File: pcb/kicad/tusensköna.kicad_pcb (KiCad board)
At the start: 2 copper layers, 93.2 x 50.5 mm, 36 parts, among them J1 AudioJack3, J2 AudioJack3, J3 Micro_SD_Card, SW1 SW_Push, SW2 SW_Push, U1 Electrosmith_Daisy_Seed_Rev4

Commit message: issues fixed
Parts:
- removed 3V3A1, 3V3D1, A0, A6, GND1, MI1, MO1, SCK1, SCL1, SDA1, SS1, VIN1: Conn_01x01, Connector_Wire:SolderWire-0.5sqmm_1x01_D0.9mm_OD2.1mm
- added J4: Conn_01x12_Pin, Connector_PinHeader_2.54mm:PinHeader_1x12_P2.54mm_Vertical, F.Cu at (156.0, 26.0)
- added JP1: Jumper_2_Bridged, Connector_PinHeader_2.54mm:PinHeader_1x02_P2.54mm_Vertical, F.Cu at (164.5, 28.6)
- added JP2: Jumper_2_Bridged, Connector_PinHeader_2.54mm:PinHeader_1x02_P2.54mm_Vertical, F.Cu at (160.7, 28.6)
- added R10: 4.7k, Resistor_SMD:R_0805_2012Metric, B.Cu at (143.3, 33.7)
- added R9: 4.7k, Resistor_SMD:R_0805_2012Metric, B.Cu at (145.9, 33.8)
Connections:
- U1 pad 12: /SDA -> Net-(JP1-A)
- U1 pad 13: /SCL -> Net-(JP2-A)
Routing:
- net Net-(JP1-A): track 0.00 -> 48.7 mm
- net Net-(JP2-A): track 0.00 -> 48.6 mm, vias 0 -> 1
- net /SDA: track 17.4 -> 37.4 mm
- net /SCL: track 17.8 -> 26.8 mm
- net /SPI_CS: track 15.8 -> 20.7 mm
- net /SPI_SCK: track 16.2 -> 20.4 mm
- net /SPI_POCI: track 16.6 -> 19.1 mm
- net /SPI_PICO: track 17.0 -> 19.4 mm
- net /VIN: track 60.5 -> 62.7 mm
- net /3V3D: track 107.5 -> 108.4 mm
- net /ADC6: track 44.1 -> 43.5 mm

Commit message: pullup
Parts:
- R10, R9: moved to F.Cu
- moved R9 18.6 mm to (164.5, 33.7), turned to -90 degrees
- moved R10 17.3 mm to (160.7, 33.7), turned to -90 degrees
- moved JP1 2.54 mm to (164.5, 26.0), turned to 0 degrees
- moved JP2 2.54 mm to (160.7, 26.0), turned to 0 degrees
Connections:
- JP1 pad 1: Net-(JP1-A) -> /3V3D
- JP1 pad 2: /SCL -> Net-(JP1-B)
- JP2 pad 1: Net-(JP2-A) -> /3V3D
- JP2 pad 2: /SDA -> Net-(JP2-B)
- R10 pad 1: Net-(JP2-A) -> Net-(JP2-B)
- R9 pad 1: Net-(JP1-A) -> Net-(JP1-B)
- U1 pad 12: Net-(JP1-A) -> /SCL
- U1 pad 13: Net-(JP2-A) -> /SDA
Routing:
- net Net-(JP1-A): track 48.7 -> 0.00 mm
- net Net-(JP2-A): track 48.6 -> 0.00 mm, vias 1 -> 0
- net /3V3D: track 108.4 -> 138.8 mm
- net /SDA: track 37.4 -> 26.5 mm
- net Net-(JP1-B): track 0.00 -> 4.17 mm
- net Net-(JP2-B): track 0.00 -> 4.16 mm

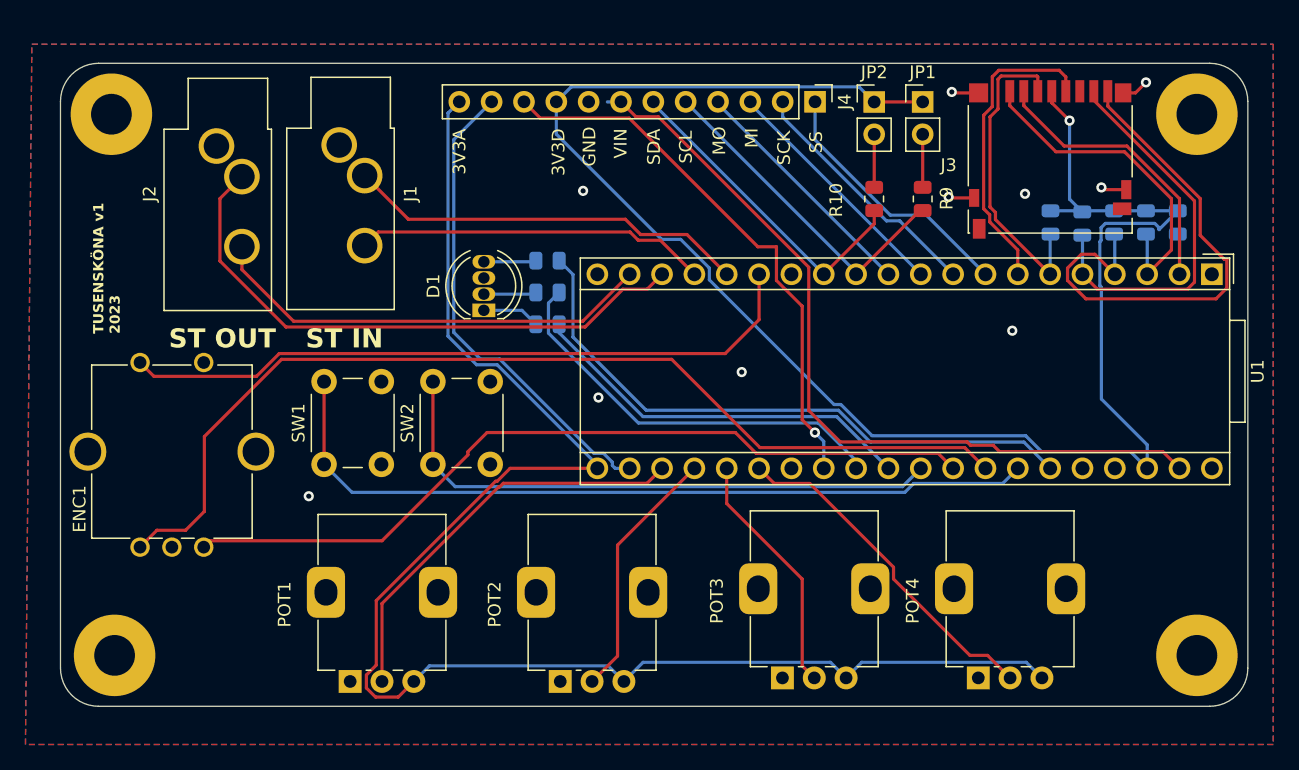
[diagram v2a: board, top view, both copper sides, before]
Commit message: fixed gnd planes and cleanup
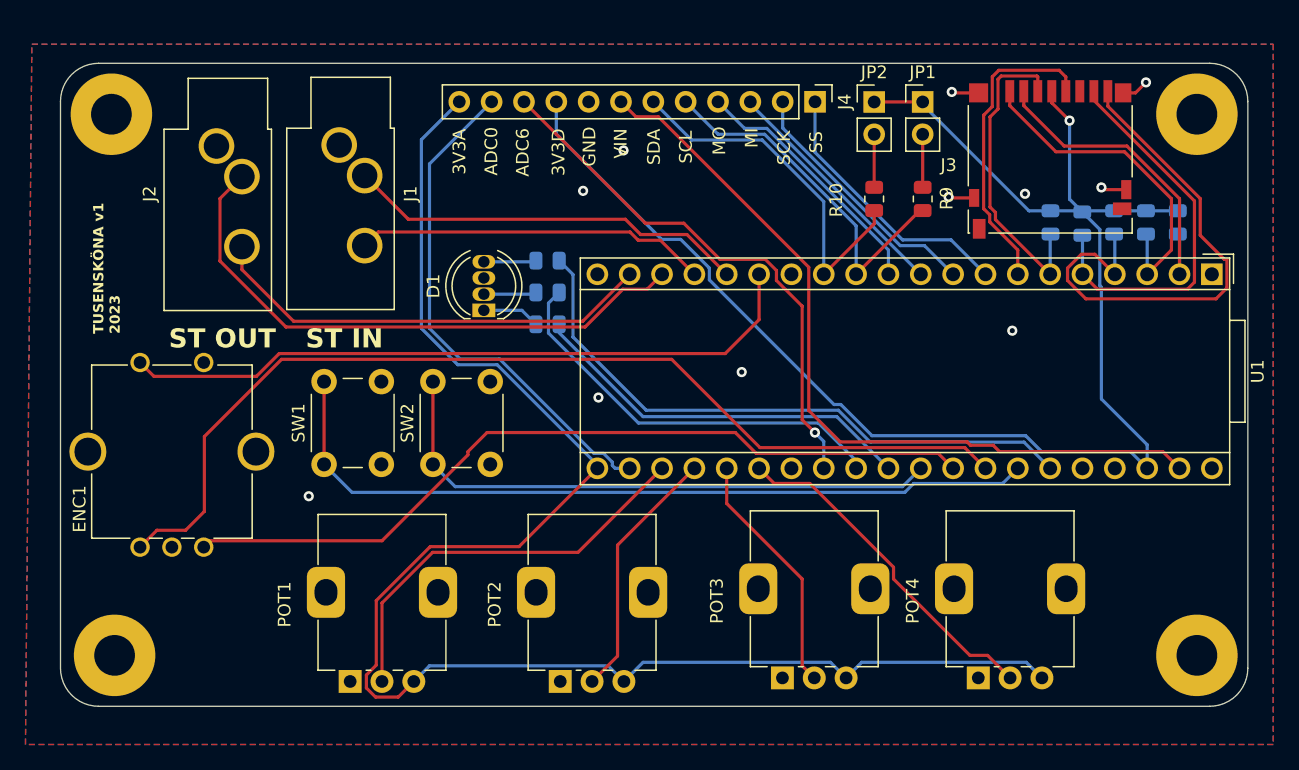
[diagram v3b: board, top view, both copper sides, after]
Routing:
- net /3V3D: track 138.8 -> 121.3 mm
- net /SDA: track 26.5 -> 29.1 mm
- net /3V3A: track 120.8 -> 123.4 mm
- net /ADC0: track 37.7 -> 40.2 mm
- net /SCL: track 26.7 -> 28.5 mm
- net /ADC6: track 43.5 -> 42.4 mm
- net /SPI_PICO: track 19.4 -> 20.3 mm
- net /SPI_CS: track 20.7 -> 21.3 mm
- net /SPI_SCK: track 20.4 -> 20.9 mm
- net /AGND: vias 10 -> 11
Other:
- board text added: "ADC0"
- board text added: "ADC6"

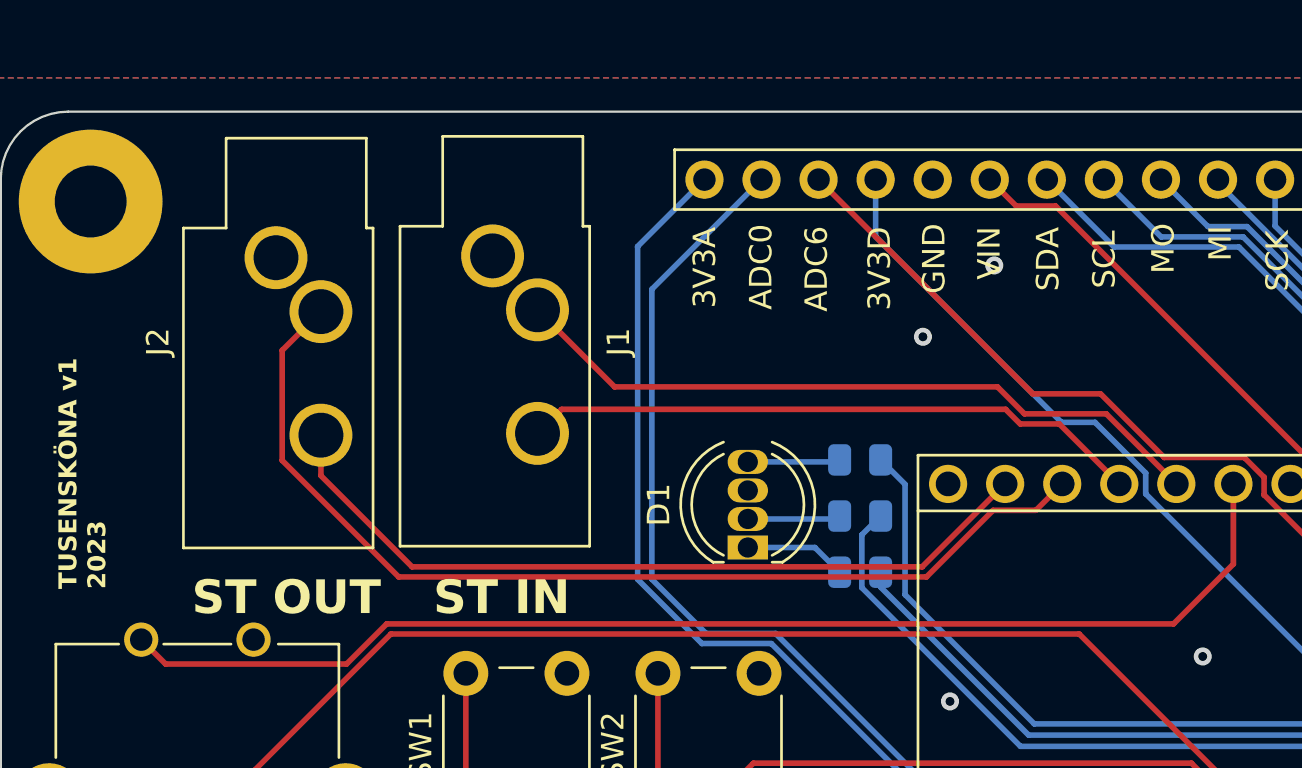
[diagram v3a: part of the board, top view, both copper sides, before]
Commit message: stereo connectors outside of the board
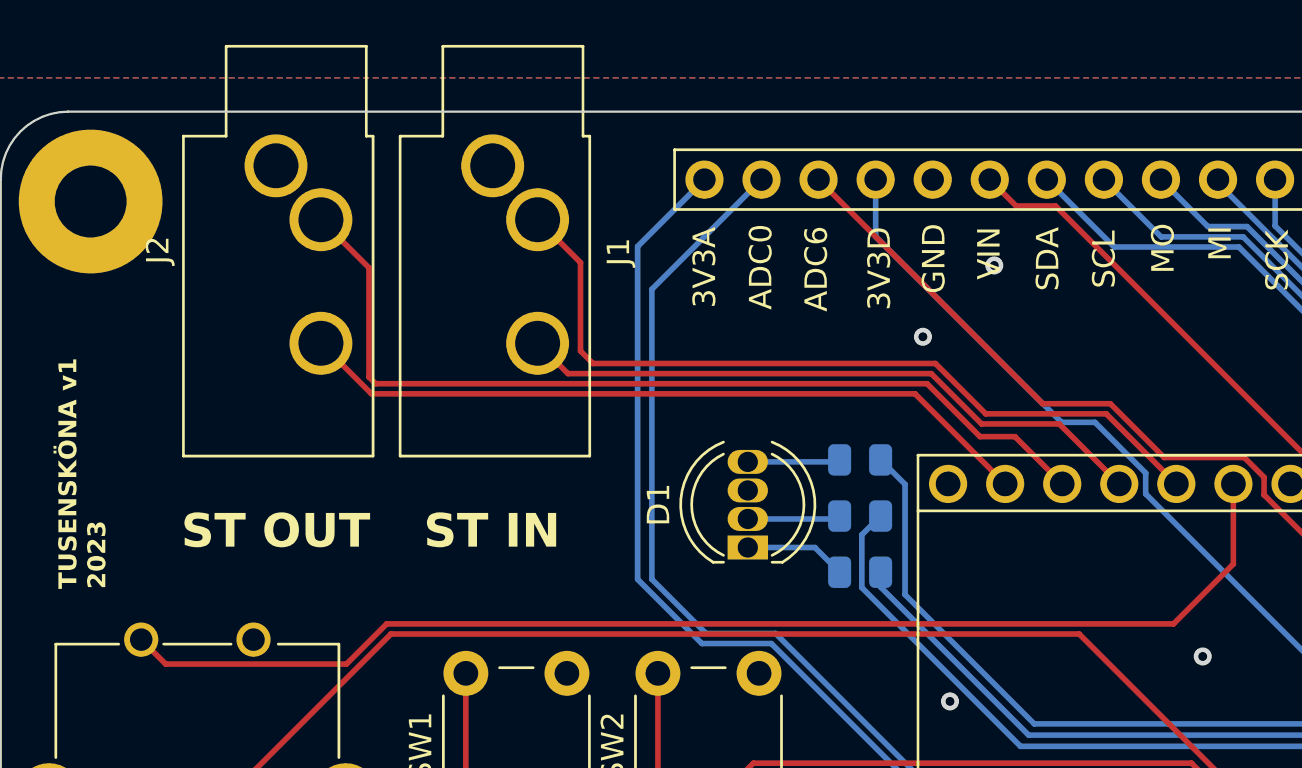
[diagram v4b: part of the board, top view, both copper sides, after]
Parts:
- moved J2 4.09 mm to (109.0, 25.4)
- moved J1 4.01 mm to (118.6, 25.4)
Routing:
- net /STEREO OUT L: track 45.9 -> 40.7 mm
- net /STEREO IN L: track 31.6 -> 35.6 mm
- net /STEREO OUT R: track 35.5 -> 33.0 mm
- net /STEREO IN R: track 27.7 -> 28.5 mm
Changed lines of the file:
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@@
   )
   (footprint "Connector_Audio:Jack_3.5mm_CUI_SJ1-3533NG_Horizontal_CircularHoles" (layer "F.Cu")
-    (at 118.64 29.42)
+    (at 118.645 25.41)
     (descr "TRS 3.5mm, horizontal, through-hole, , circular holeshttps://www.cui.com/product/resource/sj1-353xng.pdf")
     (tags "TRS audio jack stereo horizontal circular")
@@
   )
   (footprint "Connector_Audio:Jack_3.5mm_CUI_SJ1-3533NG_Horizontal_CircularHoles" (layer "F.Cu")
-    (at 109 29.5)
+    (at 109 25.41)
     (descr "TRS 3.5mm, horizontal, through-hole, , circular holeshttps://www.cui.com/product/resource/sj1-353xng.pdf")
     (tags "TRS audio jack stereo horizontal circular")
@@
     (effects (font (size 1 1) (thickness 0.15)) (justify left bottom))
   )
-  (gr_text "ST IN\n" (at 116 45.5) (layer "F.SilkS" knockout)
+  (gr_text "ST IN\n" (at 115.57 42.545) (layer "F.SilkS" knockout)
     (effects (font (size 1.5 1.5) (thickness 0.3) bold) (justify left bottom))
   )
@@
     (effects (font (size 0.8 0.8) (thickness 0.125) bold) (justify left bottom))
   )
-  (gr_text "ST OUT" (at 105.25 45.5) (layer "F.SilkS" knockout)
+  (gr_text "ST OUT" (at 104.775 42.545) (layer "F.SilkS" knockout)
     (effects (font (size 1.5 1.5) (thickness 0.3) bold) (justify left bottom))
   )
@@
   (segment (start 131.048833 46.675) (end 138.915 54.541167) (width 0.25) (layer "B.Cu") (net 7))
   (segment (start 139.775 70.325) (end 141 71.55) (width 0.25) (layer "B.Cu") (net 7))
+  (segment (start 140.592792 36.45) (end 145.955 36.45) (width 0.25) (layer "F.Cu") (net 8))
+  (segment (start 120.645 27.81) (end 122.555 29.72) (width 0.25) (layer "F.Cu") (net 8))
+  (segment (start 138.352792 34.21) (end 140.592792 36.45) (width 0.25) (layer "F.Cu") (net 8))
+  (segment (start 122.555 33.655) (end 123.11 34.21) (width 0.25) (layer "F.Cu") (net 8))
   (segment (start 145.955 36.45) (end 149.075 39.57) (width 0.25) (layer "F.Cu") (net 8))
-  (segment (start 141.113604 35.25) (end 142.313604 36.45) (width 0.25) (layer "F.Cu") (net 8))
-  (segment (start 124.07 35.25) (end 141.113604 35.25) (width 0.25) (layer "F.Cu") (net 8))
-  (segment (start 120.64 31.82) (end 124.07 35.25) (width 0.25) (layer "F.Cu") (net 8))
-  (segment (start 142.313604 36.45) (end 145.955 36.45) (width 0.25) (layer "F.Cu") (net 8))
-  (segment (start 121.71 36.25) (end 141.477208 36.25) (width 0.25) (layer "F.Cu") (net 9))
-  (segment (start 142.127208 36.9) (end 143.865 36.9) (width 0.25) (layer "F.Cu") (net 9))
+  (segment (start 122.555 29.72) (end 122.555 33.655) (width 0.25) (layer "F.Cu") (net 8))
+  (segment (start 123.11 34.21) (end 138.352792 34.21) (width 0.25) (layer "F.Cu") (net 8))
+  (segment (start 120.645 33.31) (end 121.995 34.66) (width 0.25) (layer "F.Cu") (net 9))
+  (segment (start 138.166396 34.66) (end 140.406396 36.9) (width 0.25) (layer "F.Cu") (net 9))
   (segment (start 143.865 36.9) (end 146.535 39.57) (width 0.25) (layer "F.Cu") (net 9))
-  (segment (start 120.64 37.32) (end 121.71 36.25) (width 0.25) (layer "F.Cu") (net 9))
-  (segment (start 141.477208 36.25) (end 142.127208 36.9) (width 0.25) (layer "F.Cu") (net 9))
-  (segment (start 109.275 33.625) (end 109.275 38.525) (width 0.25) (layer "F.Cu") (net 10))
-  (segment (start 114.46 43.71) (end 137.951396 43.71) (width 0.25) (layer "F.Cu") (net 10))
-  (segment (start 137.951396 43.71) (end 140.916396 40.745) (width 0.25) (layer "F.Cu") (net 10))
-  (segment (start 140.916396 40.745) (end 142.82 40.745) (width 0.25) (layer "F.Cu") (net 10))
-  (segment (start 142.82 40.745) (end 143.995 39.57) (width 0.25) (layer "F.Cu") (net 10))
-  (segment (start 109.275 38.525) (end 114.46 43.71) (width 0.25) (layer "F.Cu") (net 10))
-  (segment (start 111 31.9) (end 109.275 33.625) (width 0.25) (layer "F.Cu") (net 10))
-  (segment (start 137.765 43.26) (end 141.455 39.57) (width 0.25) (layer "F.Cu") (net 11))
-  (segment (start 111 37.4) (end 111 39.203123) (width 0.25) (layer "F.Cu") (net 11))
-  (segment (start 111 39.203123) (end 115.056877 43.26) (width 0.25) (layer "F.Cu") (net 11))
-  (segment (start 115.056877 43.26) (end 137.765 43.26) (width 0.25) (layer "F.Cu") (net 11))
+  (segment (start 140.406396 36.9) (end 143.865 36.9) (width 0.25) (layer "F.Cu") (net 9))
+  (segment (start 121.995 34.66) (end 138.166396 34.66) (width 0.25) (layer "F.Cu") (net 9))
+  (segment (start 141.89 37.465) (end 143.995 39.57) (width 0.25) (layer "F.Cu") (net 10))
+  (segment (start 113.140698 29.950698) (end 113.140698 34.814302) (width 0.25) (layer "F.Cu") (net 10))
+  (segment (start 113.140698 34.814302) (end 113.436396 35.11) (width 0.25) (layer "F.Cu") (net 10))
+  (segment (start 111 27.81) (end 113.140698 29.950698) (width 0.25) (layer "F.Cu") (net 10))
+  (segment (start 140.335 37.465) (end 141.89 37.465) (width 0.25) (layer "F.Cu") (net 10))
+  (segment (start 137.98 35.11) (end 140.335 37.465) (width 0.25) (layer "F.Cu") (net 10))
+  (segment (start 113.436396 35.11) (end 137.98 35.11) (width 0.25) (layer "F.Cu") (net 10))
+  (segment (start 111 33.31) (end 113.25 35.56) (width 0.25) (layer "F.Cu") (net 11))
+  (segment (start 137.445 35.56) (end 141.455 39.57) (width 0.25) (layer "F.Cu") (net 11))
+  (segment (start 113.25 35.56) (end 137.445 35.56) (width 0.25) (layer "F.Cu") (net 11))
   (segment (start 180.455 32.925) (end 178.675 32.925) (width 0.25) (layer "F.Cu") (net 12))
   (segment (start 168.855 25.325) (end 166.825 25.325) (width 0.25) (layer "F.Cu") (net 12))
@@
   (segment (start 138.645229 53.635) (end 131.235229 46.225) (width 0.25) (layer "B.Cu") (net 18))
   (segment (start 140.09 54.59) (end 140.09 54.323299) (width 0.25) (layer "B.Cu") (net 18))
-  (segment (start 142.684889 35.56) (end 145.701396 35.56) (width 0.25) (layer "F.Cu") (net 20))
+  (segment (start 152.101701 38.395) (end 152.98 39.273299) (width 0.25) (layer "F.Cu") (net 20))
   (segment (start 152.981649 40.058351) (end 155 42.076701) (width 0.25) (layer "F.Cu") (net 20))
-  (segment (start 152.98 40.056702) (end 152.981649 40.058351) (width 0.25) (layer "F.Cu") (net 20))
+  (segment (start 146.141396 36) (end 148.536396 38.395) (width 0.25) (layer "F.Cu") (net 20))
+  (segment (start 148.536396 38.395) (end 152.101701 38.395) (width 0.25) (layer "F.Cu") (net 20))
   (segment (start 155 42.076701) (end 155 51) (width 0.25) (layer "F.Cu") (net 20))
   (segment (start 152.98 39.273299) (end 152.98 40.056702) (width 0.25) (layer "F.Cu") (net 20))
-  (segment (start 145.701396 35.56) (end 148.536396 38.395) (width 0.25) (layer "F.Cu") (net 20))
-  (segment (start 133.150276 26.025387) (end 142.684889 35.56) (width 0.25) (layer "F.Cu") (net 20))
+  (segment (start 143.124889 36) (end 146.141396 36) (width 0.25) (layer "F.Cu") (net 20))
+  (segment (start 152.98 40.056702) (end 152.981649 40.058351) (width 0.25) (layer "F.Cu") (net 20))
+  (segment (start 133.150276 26.025387) (end 143.124889 36) (width 0.25) (layer "F.Cu") (net 20))
   (segment (start 155 51) (end 156 52) (width 0.25) (layer "F.Cu") (net 20))
-  (segment (start 152.101701 38.395) (end 152.98 39.273299) (width 0.25) (layer "F.Cu") (net 20))
   (segment (start 152.98 40.056701) (end 152.981649 40.058351) (width 0.25) (layer "F.Cu") (net 20))
-  (segment (start 148.536396 38.395) (end 152.101701 38.395) (width 0.25) (layer "F.Cu") (net 20))
   (via (at 156 52) (size 0.8) (drill 0.4) (layers "F.Cu" "B.Cu") (net 20))
   (segment (start 156.695 52.695) (end 156.695 54.81) (width 0.25) (layer "B.Cu") (net 20))
